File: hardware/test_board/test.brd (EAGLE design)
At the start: 70.5 x 75.9 mm, 27 parts, among them IC3 74HCT573N, IC5 7805DT, J2 POWER_JACKSLT

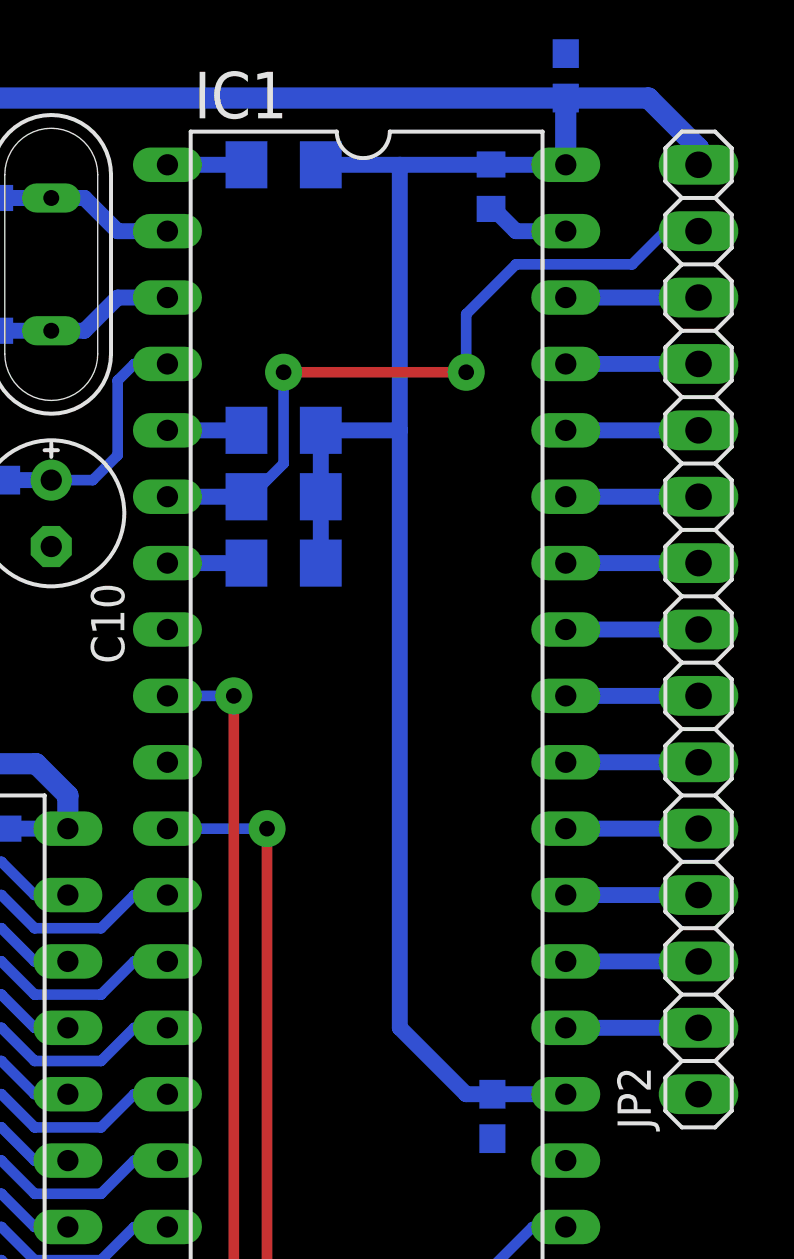
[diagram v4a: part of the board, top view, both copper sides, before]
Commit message: Diode aded at RST line
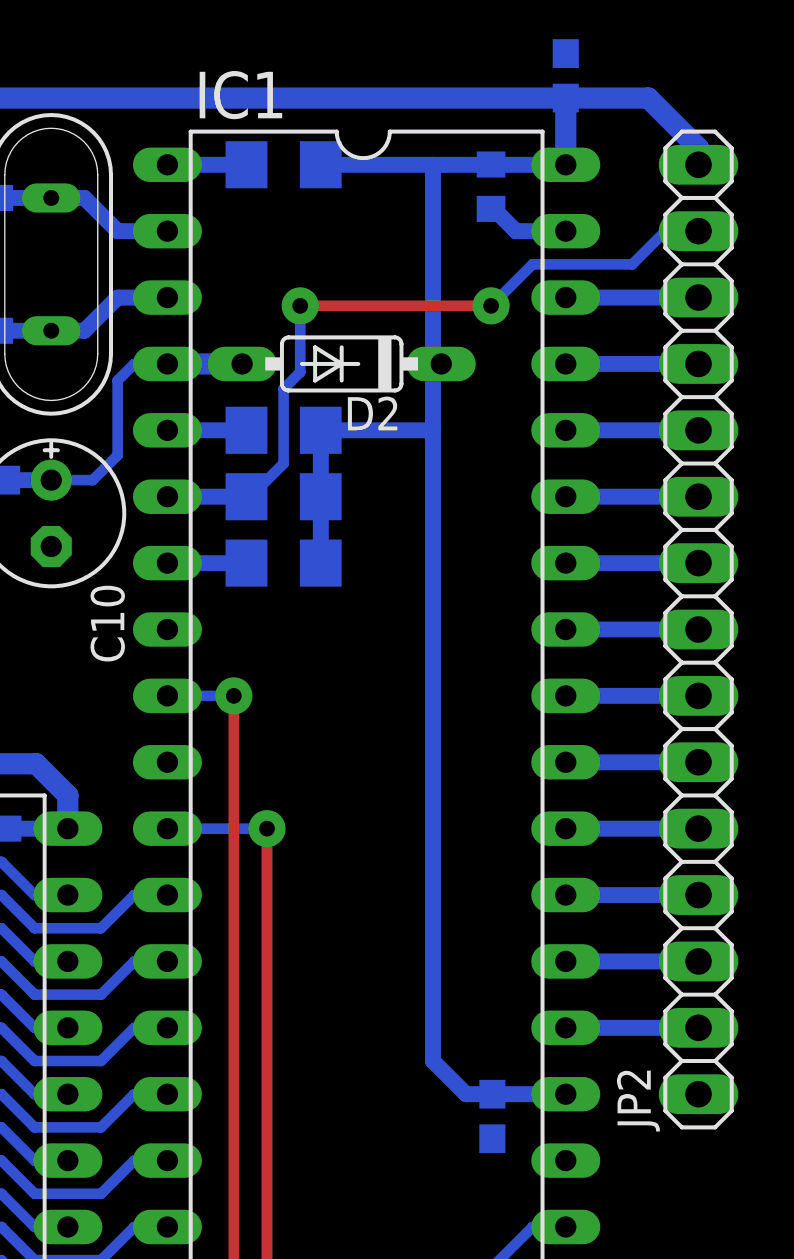
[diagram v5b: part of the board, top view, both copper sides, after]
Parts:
- added D2: 1N4148DO35-7, diode:DO35-7
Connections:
- net !RESET: now also D2.A
- net VCC: now also D2.C
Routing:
- net !RESET: track 9.65 -> 12.5 mm
- net VCC: track 207.0 -> 208.0 mm
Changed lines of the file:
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@@
 <element name="IC2" library="memory" package="DIL24" value="" x="18.415" y="19.05" rot="R90"/>
 <element name="C11" library="rcl" package="C0603" value="" x="58.1533" y="32.1691" rot="MR270"/>
+<element name="D2" library="diode" package="DO35-7" value="1N4148DO35-7" x="52.3875" y="60.96" rot="R180"/>
 </elements>
 <signals>
@@
 <wire x1="51.587" y1="58.42" x2="51.587" y2="55.88" width="0.6096" layer="16"/>
 <wire x1="51.587" y1="55.88" x2="51.587" y2="53.34" width="0.6096" layer="16"/>
-<wire x1="51.587" y1="68.58" x2="54.61" y2="68.58" width="0.6096" layer="16"/>
-<wire x1="54.61" y1="68.58" x2="58.42" y2="68.58" width="0.6096" layer="16"/>
+<wire x1="51.587" y1="68.58" x2="55.88" y2="68.58" width="0.6096" layer="16"/>
+<wire x1="55.88" y1="68.58" x2="58.42" y2="68.58" width="0.6096" layer="16"/>
 <wire x1="58.42" y1="68.58" x2="60.96" y2="68.58" width="0.6096" layer="16"/>
 <wire x1="58.1025" y1="68.5918" x2="58.4082" y2="68.5918" width="0.6096" layer="16"/>
@@
 <wire x1="8.89" y1="5.08" x2="10.795" y2="5.08" width="0.8128" layer="16"/>
 <wire x1="26.530234375" y1="45.6625" x2="26.530234375" y2="67.805234375" width="0.8128" layer="16"/>
-<wire x1="54.61" y1="68.58" x2="54.61" y2="58.42" width="0.6096" layer="16"/>
-<wire x1="54.61" y1="58.42" x2="54.61" y2="35.56" width="0.6096" layer="16"/>
-<wire x1="54.61" y1="35.56" x2="57.15" y2="33.02" width="0.6096" layer="16"/>
+<wire x1="55.88" y1="58.42" x2="55.88" y2="34.29" width="0.6096" layer="16"/>
+<wire x1="55.88" y1="34.29" x2="57.15" y2="33.02" width="0.6096" layer="16"/>
 <contactref element="C6" pad="1"/>
 <contactref element="C8" pad="+"/>
@@
 <wire x1="64.1214" y1="71.1336" x2="66.04" y2="69.215" width="0.8128" layer="16"/>
 <contactref element="JP2" pad="15"/>
-<wire x1="51.587" y1="58.42" x2="54.61" y2="58.42" width="0.6096" layer="16"/>
+<wire x1="51.587" y1="58.42" x2="55.88" y2="58.42" width="0.6096" layer="16"/>
 <contactref element="IC2" pad="24"/>
 <wire x1="66.04" y1="69.215" x2="66.04" y2="68.58" width="0.8128" layer="16"/>
@@
 <wire x1="58.1533" y1="33.0191" x2="58.4191" y2="33.0191" width="0.4064" layer="16"/>
 <wire x1="58.4191" y1="33.0191" x2="58.42" y2="33.02" width="0.4064" layer="16"/>
+<contactref element="D2" pad="C"/>
+<wire x1="55.88" y1="58.42" x2="55.88" y2="60.96" width="0.6096" layer="16"/>
+<wire x1="55.88" y1="60.96" x2="55.88" y2="68.58" width="0.6096" layer="16"/>
+<wire x1="56.1975" y1="60.96" x2="55.88" y2="60.96" width="0.4064" layer="16"/>
 </signal>
 <signal name="GND">
@@
 <wire x1="42.8625" y1="56.515" x2="43.815" y2="57.4675" width="0.4064" layer="16"/>
 <wire x1="39.585" y1="56.515" x2="41.275" y2="56.515" width="0.6096" layer="16"/>
+<contactref element="D2" pad="A"/>
+<wire x1="45.72" y1="60.96" x2="48.5775" y2="60.96" width="0.8128" layer="16"/>
 </signal>
 <signal name="N$9">
@@
 <contactref element="R5" pad="1"/>
 <wire x1="45.72" y1="55.88" x2="48.743" y2="55.88" width="0.6096" layer="16"/>
-<via x="50.165" y="60.6425" extent="1-16" drill="0.6" diameter="1.4224" shape="octagon"/>
-<wire x1="50.165" y1="60.6425" x2="57.15" y2="60.6425" width="0.4064" layer="1"/>
-<via x="57.15" y="60.6425" extent="1-16" drill="0.6" diameter="1.4224" shape="octagon"/>
-<wire x1="57.15" y1="60.6425" x2="57.15" y2="62.865" width="0.4064" layer="16"/>
-<wire x1="57.15" y1="62.865" x2="59.055" y2="64.77" width="0.4064" layer="16"/>
-<wire x1="59.055" y1="64.77" x2="63.5" y2="64.77" width="0.4064" layer="16"/>
+<via x="50.8" y="63.1825" extent="1-16" drill="0.6" diameter="1.4224" shape="octagon"/>
+<wire x1="50.8" y1="63.1825" x2="58.1025" y2="63.1825" width="0.4064" layer="1"/>
+<via x="58.1025" y="63.1825" extent="1-16" drill="0.6" diameter="1.4224" shape="octagon"/>
 <wire x1="63.5" y1="64.77" x2="64.77" y2="66.04" width="0.4064" layer="16"/>
 <wire x1="64.77" y1="66.04" x2="66.04" y2="66.04" width="0.4064" layer="16"/>
-<wire x1="50.165" y1="60.6425" x2="50.165" y2="57.15" width="0.4064" layer="16"/>
 <wire x1="48.743" y1="55.88" x2="48.895" y2="55.88" width="0.4064" layer="16"/>
 <wire x1="48.895" y1="55.88" x2="50.165" y2="57.15" width="0.4064" layer="16"/>
+<wire x1="50.165" y1="57.15" x2="50.165" y2="60.0075" width="0.4064" layer="16"/>
+<wire x1="50.165" y1="60.0075" x2="50.8" y2="60.6425" width="0.4064" layer="16"/>
+<wire x1="50.8" y1="63.1825" x2="50.8" y2="60.6425" width="0.4064" layer="16"/>
+<wire x1="63.5" y1="64.77" x2="59.69" y2="64.77" width="0.4064" layer="16"/>
+<wire x1="59.69" y1="64.77" x2="58.1025" y2="63.1825" width="0.4064" layer="16"/>
 </signal>
 <signal name="A11">
